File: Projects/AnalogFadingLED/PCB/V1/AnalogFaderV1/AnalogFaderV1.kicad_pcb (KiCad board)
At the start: 2 copper layers, 24.1 x 19.1 mm, 22 parts, among them J1 USB_B_Micro, SW1 SW_DIP_x03, U1 LMV324A

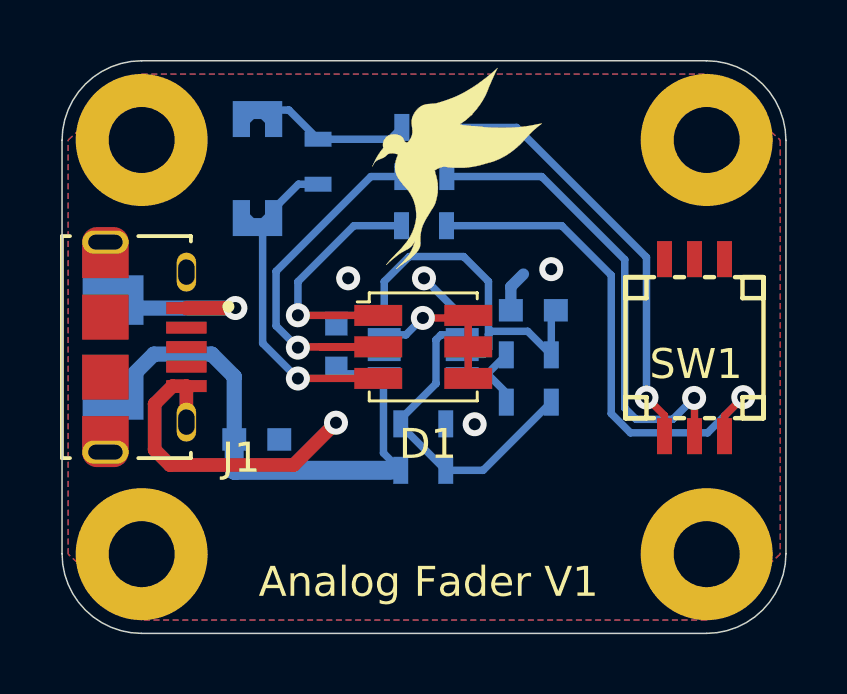
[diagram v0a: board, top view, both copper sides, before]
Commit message: Updated PCB to REV 1.1
Fixed inverted footprint for LMV358
Added trace length to switch ground connection for easier soldering
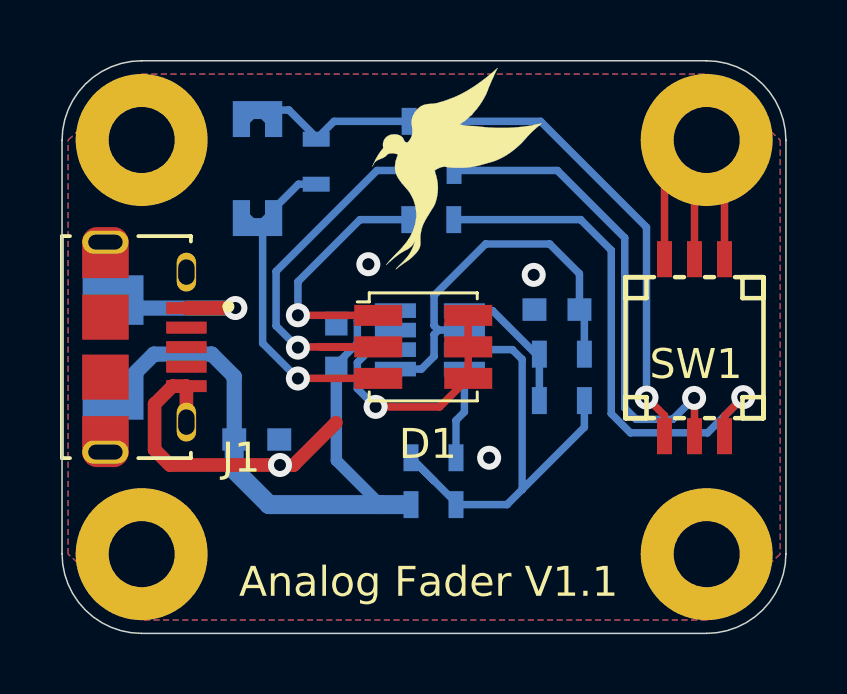
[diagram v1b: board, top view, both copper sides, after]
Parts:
- R8: value 110 or 63 -> 0
- U1: value LMV324A -> LMV358; footprint digikey-footprints:SOT-23-8 -> LMV358_sot_23_8:SOT_23_8_LMV358
- moved R1 1.19 mm to (122.6, 54.1)
- moved R2 1.18 mm to (122.6, 52.6)
- moved R3 1.10 mm to (126.9, 50.7)
- moved R4 1.10 mm to (126.9, 49.1)
- moved C1 0.79 mm to (126.8, 47.6)
- moved R7 0.32 mm to (122.6, 41.4)
- moved R6 0.32 mm to (122.6, 43.0)
- moved R5 0.32 mm to (122.6, 44.6)
- moved U1 0.27 mm to (122.5, 48.6), turned to 180 degrees
- moved R8 0.06 mm to (118.7, 42.7)
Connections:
- J1 pad S1: GND -> (no net)
- J1 pad S3: GND -> (no net)
- J1 pad S6: GND -> (no net)
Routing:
- net GND: track 14.4 -> 26.9 mm, vias 5 -> 4
- net Net-(R1-Pad2): track 10.9 -> 15.9 mm
- net VCC: track 19.2 -> 23.6 mm
- net Net-(D1-Pad4): track 5.82 -> 9.53 mm
- net Net-(R3-Pad1): track 2.93 -> 4.65 mm
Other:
- board text added: "Analog Fader V1.1"
- board text removed: "Analog Fader V1"
